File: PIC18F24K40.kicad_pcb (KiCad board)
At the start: 2 copper layers, 22 x 34.5 mm, 16 parts, among them J1 Conn_01x13, J2 Conn_01x13, J3 ICSP, J4 USB_B_Micro, SW1 SW_SPST, U1 FT231XQ, U2 PIC18F24K40-I_ML

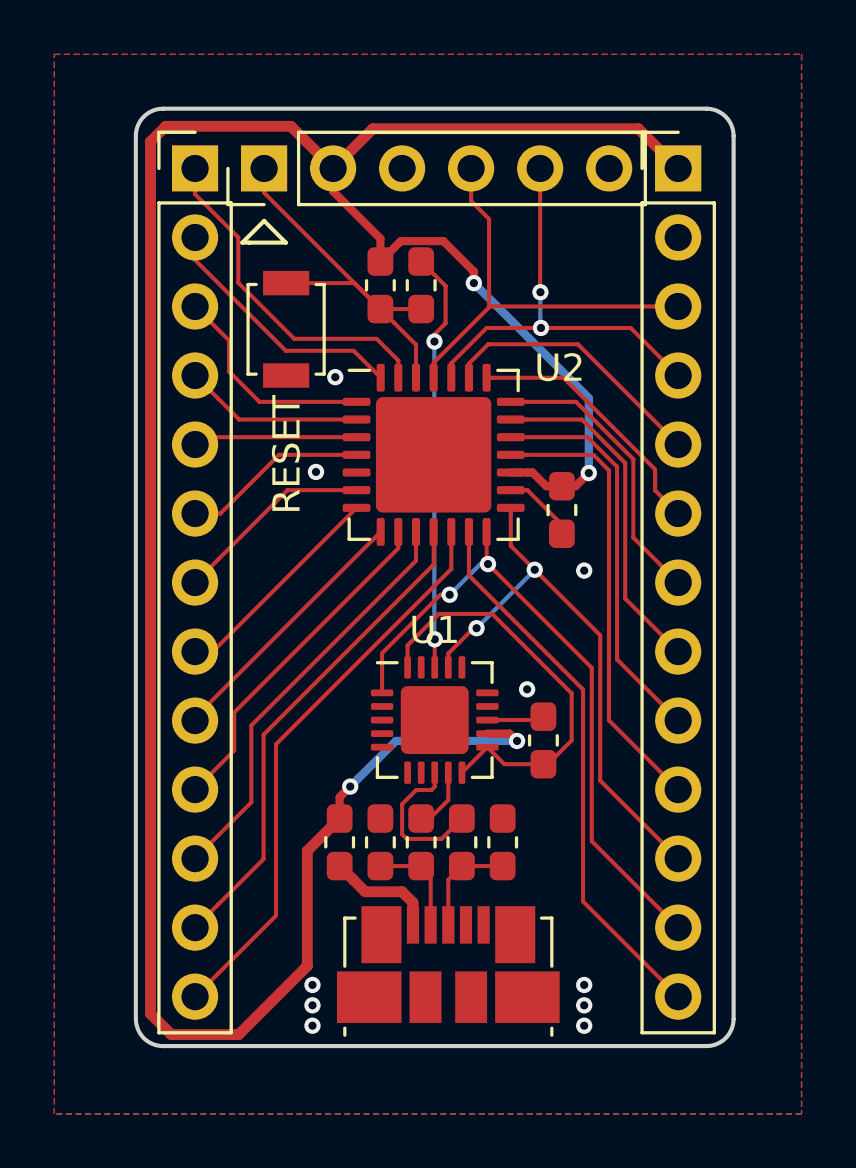
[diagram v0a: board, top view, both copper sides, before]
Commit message: LED and phototransistor added
I've added an LED for output and phototransistor for input. No button
though.
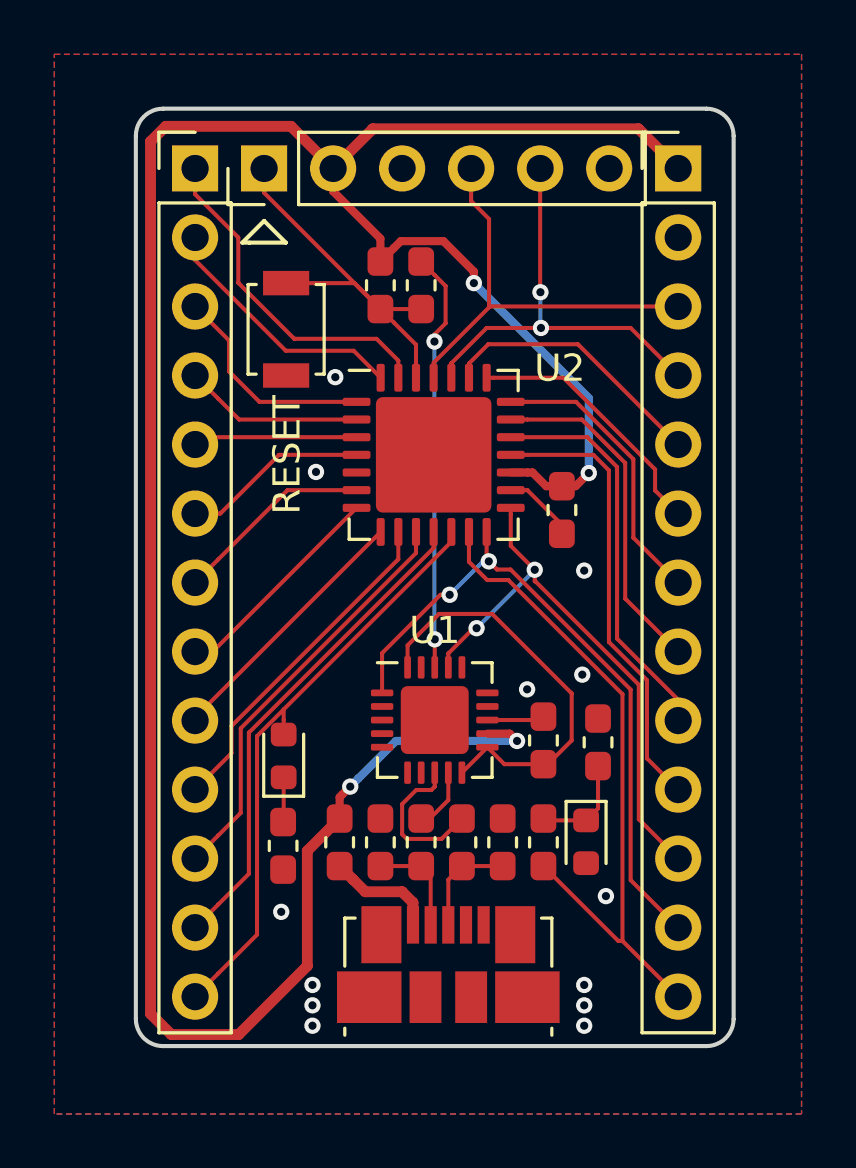
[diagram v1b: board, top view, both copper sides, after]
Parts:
- added C6: 0.01uf, _PIC18F24K40:C_0603_1608Metric_Pad1.05x0.95mm_HandSolder, F.Cu at (121.5, 97.3)
- added D1: blue, _PIC18F24K40:LED_0603_1608Metric, F.Cu at (109.9, 97.8)
- added Q1: Q_Photo_NPN, _PIC18F24K40:LED_0603_1608Metric, F.Cu at (121.1, 101.0)
- added R4: 360, _PIC18F24K40:R_0603_1608Metric_Pad1.05x0.95mm_HandSolder, F.Cu at (109.9, 101.1)
- added R5: 10k, _PIC18F24K40:R_0603_1608Metric_Pad1.05x0.95mm_HandSolder, F.Cu at (119.5, 101.0)
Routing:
- net /RC5: track 20.3 -> 24.8 mm
- net Net-(C6-Pad1): track 0.00 -> 3.78 mm
- net Net-(D1-Pad1): track 0.00 -> 1.66 mm
- net /RC4: track 21.0 -> 21.9 mm
- net GND: vias 10 -> 13

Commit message: Labels added to LED/Photo transistor
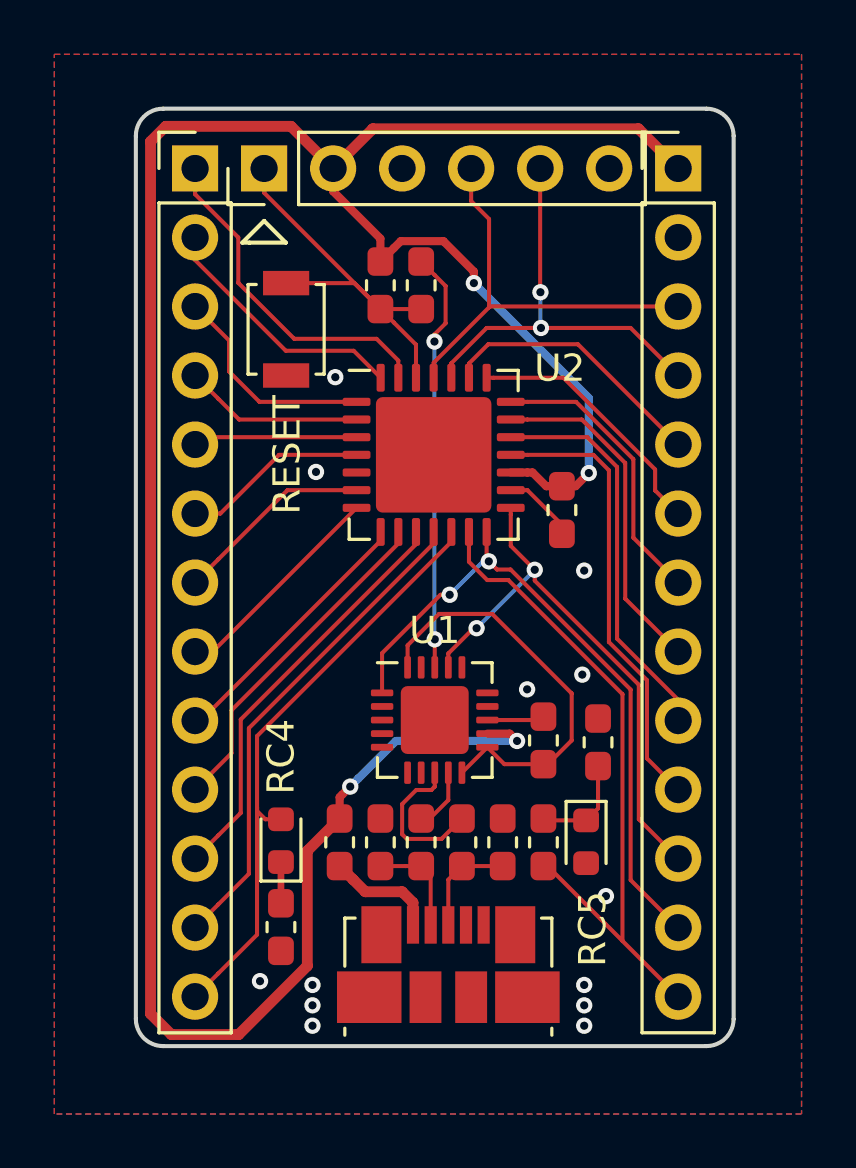
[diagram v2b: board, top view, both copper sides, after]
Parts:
- moved D1 3.12 mm to (109.8, 100.9)
- moved R4 2.99 mm to (109.8, 104.1)
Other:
- board text added: "RC4"
- board text added: "RC5"
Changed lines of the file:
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@@
   (general
     (thickness 1.6)
-    (drawings 9)
-    (tracks 253)
+    (drawings 11)
+    (tracks 256)
     (zones 0)
     (modules 21)
@@
   )
   (module _PIC18F24K40:LED_0603_1608Metric (layer F.Cu)
-    (at 109.94 97.82 90)
+    (at 109.84 100.94 90)
     (descr "LED SMD 0603 (1608 Metric), square (rectangular) end terminal, IPC_7351 nominal, (Body size source: http://www.tortai-tech.com/upload/download/2011102023233369053.pdf), generated with kicad-footprint-generator")
     (tags diode)
@@
   )
   (module _PIC18F24K40:R_0603_1608Metric_Pad1.05x0.95mm_HandSolder (layer F.Cu)
-    (at 109.92 101.13 270)
+    (at 109.84 104.12 270)
     (descr "Resistor SMD 0603 (1608 Metric), square (rectangular) end terminal, IPC_7351 nominal with elongated pad for handsoldering. (Body size source: http://www.tortai-tech.com/upload/download/2011102023233369053.pdf), generated with kicad-footprint-generator")
     (tags "resistor handsolder")
@@
       (rotate (xyz 0 0 0))
     )
+  )
+  (gr_text RC5 (at 121.31 104.19 90) (layer F.SilkS)
+    (effects (font (size 1 1) (thickness 0.15)))
+  )
+  (gr_text RC4 (at 109.84 97.85 90) (layer F.SilkS)
+    (effects (font (size 1 1) (thickness 0.15)))
   )
   (gr_arc (start 105.5 75) (end 105.5 74) (angle -90) (layer Edge.Cuts) (width 0.15))
@@
   (via (at 118.9 95.37) (size 0.6) (drill 0.3) (layers F.Cu B.Cu) (net 2))
   (via (at 111.84 83.88) (size 0.6) (drill 0.3) (layers F.Cu B.Cu) (net 2))
-  (via (at 109.85 103.56) (size 0.6) (drill 0.3) (layers F.Cu B.Cu) (net 2))
+  (via (at 109.07 106.11) (size 0.6) (drill 0.3) (layers F.Cu B.Cu) (net 2))
   (via (at 120.93 94.83) (size 0.6) (drill 0.3) (layers F.Cu B.Cu) (net 2))
   (via (at 121.8 102.98) (size 0.6) (drill 0.3) (layers F.Cu B.Cu) (net 2))
@@
   (segment (start 107.3325 93.98) (end 106.68 93.98) (width 0.15) (layer F.Cu) (net 8))
   (segment (start 112.6225 88.69) (end 107.3325 93.98) (width 0.15) (layer F.Cu) (net 8))
-  (segment (start 106.68 96.4075) (end 106.68 96.52) (width 0.15) (layer F.Cu) (net 9))
-  (segment (start 113.51 89.5775) (end 106.68 96.4075) (width 0.15) (layer F.Cu) (net 9))
+  (segment (start 106.89 96.52) (end 106.68 96.52) (width 0.15) (layer F.Cu) (net 9))
+  (segment (start 113.51 89.5775) (end 113.51 89.9) (width 0.15) (layer F.Cu) (net 9))
+  (segment (start 113.51 89.9) (end 106.89 96.52) (width 0.15) (layer F.Cu) (net 9))
   (segment (start 108.02 97.72) (end 106.68 99.06) (width 0.15) (layer F.Cu) (net 10))
-  (segment (start 108.02 96.721442) (end 108.02 97.72) (width 0.15) (layer F.Cu) (net 10))
-  (segment (start 114.16 89.5775) (end 114.16 90.581442) (width 0.15) (layer F.Cu) (net 10))
-  (segment (start 114.16 90.581442) (end 108.02 96.721442) (width 0.15) (layer F.Cu) (net 10))
-  (segment (start 114.81 89.5775) (end 114.81 90.355721) (width 0.15) (layer F.Cu) (net 11))
+  (segment (start 108.02 96.14) (end 108.02 97.72) (width 0.15) (layer F.Cu) (net 10))
+  (segment (start 114.16 89.5775) (end 114.16 90) (width 0.15) (layer F.Cu) (net 10))
+  (segment (start 114.16 90) (end 108.02 96.14) (width 0.15) (layer F.Cu) (net 10))
   (segment (start 107.529999 100.750001) (end 106.68 101.6) (width 0.15) (layer F.Cu) (net 11))
   (segment (start 108.359978 99.920022) (end 107.529999 100.750001) (width 0.15) (layer F.Cu) (net 11))
-  (segment (start 114.81 90.355721) (end 108.359978 96.805743) (width 0.15) (layer F.Cu) (net 11))
-  (segment (start 108.359978 96.805743) (end 108.359978 99.920022) (width 0.15) (layer F.Cu) (net 11))
+  (segment (start 114.81 89.5775) (end 114.81 90.03) (width 0.15) (layer F.Cu) (net 11))
+  (segment (start 108.359978 96.480022) (end 108.359978 99.920022) (width 0.15) (layer F.Cu) (net 11))
+  (segment (start 114.81 90.03) (end 108.359978 96.480022) (width 0.15) (layer F.Cu) (net 11))
   (segment (start 107.529999 103.290001) (end 106.68 104.14) (width 0.15) (layer F.Cu) (net 12))
+  (segment (start 108.659989 96.800011) (end 108.659989 102.160011) (width 0.15) (layer F.Cu) (net 12))
+  (segment (start 115.46 89.5775) (end 115.46 90) (width 0.15) (layer F.Cu) (net 12))
   (segment (start 108.659989 102.160011) (end 107.529999 103.290001) (width 0.15) (layer F.Cu) (net 12))
-  (segment (start 108.659989 96.965732) (end 108.659989 102.160011) (width 0.15) (layer F.Cu) (net 12))
-  (segment (start 115.46 89.5775) (end 115.46 90.165721) (width 0.15) (layer F.Cu) (net 12))
-  (segment (start 115.46 90.165721) (end 108.659989 96.965732) (width 0.15) (layer F.Cu) (net 12))
+  (segment (start 115.46 90) (end 108.659989 96.800011) (width 0.15) (layer F.Cu) (net 12))
   (segment (start 107.529999 105.830001) (end 106.68 106.68) (width 0.15) (layer F.Cu) (net 13))
   (segment (start 108.96 104.4) (end 107.529999 105.830001) (width 0.15) (layer F.Cu) (net 13))
-  (segment (start 108.96 97.09) (end 108.96 104.4) (width 0.15) (layer F.Cu) (net 13))
-  (segment (start 116.11 89.5775) (end 116.11 89.94) (width 0.15) (layer F.Cu) (net 13))
-  (segment (start 109.94 96.495) (end 109.94 96.11) (width 0.15) (layer F.Cu) (net 13))
-  (segment (start 109.94 97.0325) (end 109.94 96.495) (width 0.15) (layer F.Cu) (net 13))
-  (segment (start 116.11 89.94) (end 109.94 96.11) (width 0.15) (layer F.Cu) (net 13))
-  (segment (start 109.94 96.11) (end 108.96 97.09) (width 0.15) (layer F.Cu) (net 13))
   (segment (start 122.41 95.55) (end 122.41 104.63) (width 0.15) (layer F.Cu) (net 14))
   (segment (start 117.43 91.347004) (end 118.207004 91.347004) (width 0.15) (layer F.Cu) (net 14))
@@
   (segment (start 116.76 89.5775) (end 116.76 90.677004) (width 0.15) (layer F.Cu) (net 14))
   (segment (start 116.76 90.677004) (end 117.43 91.347004) (width 0.15) (layer F.Cu) (net 14))
-  (segment (start 122.255 104.63) (end 122.41 104.63) (width 0.15) (layer F.Cu) (net 14))
-  (segment (start 119.5 101.875) (end 122.255 104.63) (width 0.15) (layer F.Cu) (net 14))
+  (segment (start 121.77 103.99) (end 122.41 104.63) (width 0.15) (layer F.Cu) (net 14))
+  (segment (start 119.5 101.875) (end 119.655 101.875) (width 0.15) (layer F.Cu) (net 14))
+  (segment (start 119.655 101.875) (end 121.77 103.99) (width 0.15) (layer F.Cu) (net 14))
   (via (at 116.05 91.89) (size 0.6) (drill 0.3) (layers F.Cu B.Cu) (net 15))
   (segment (start 115.71 91.89) (end 116.05 91.89) (width 0.15) (layer F.Cu) (net 15))
@@
   (segment (start 117.04 93.12) (end 119.18 90.98) (width 0.15) (layer B.Cu) (net 16))
   (segment (start 119.18 90.97) (end 118.2975 90.0875) (width 0.15) (layer F.Cu) (net 16))
-  (segment (start 119.18 91.394264) (end 119.18 90.97) (width 0.15) (layer F.Cu) (net 16))
-  (segment (start 119.204264 91.394264) (end 119.18 91.394264) (width 0.15) (layer F.Cu) (net 16))
-  (segment (start 123.010022 95.200022) (end 119.204264 91.394264) (width 0.15) (layer F.Cu) (net 16))
+  (segment (start 123.010022 95.200022) (end 119.18 91.37) (width 0.15) (layer F.Cu) (net 16))
   (segment (start 124.46 101.6) (end 123.010022 100.150022) (width 0.15) (layer F.Cu) (net 16))
+  (segment (start 119.18 91.37) (end 119.18 90.97) (width 0.15) (layer F.Cu) (net 16))
   (segment (start 123.010022 100.150022) (end 123.010022 95.200022) (width 0.15) (layer F.Cu) (net 16))
   (segment (start 118.91 86.74) (end 118.2975 86.74) (width 0.15) (layer F.Cu) (net 17))
@@
   (segment (start 114.7 104.04) (end 114.7 103.22) (width 0.4) (layer F.Cu) (net 45))
   (segment (start 114.7 103.22) (end 114.3 102.82) (width 0.4) (layer F.Cu) (net 45))
-  (segment (start 109.94 100.235) (end 109.92 100.255) (width 0.15) (layer F.Cu) (net 46))
-  (segment (start 109.94 98.6075) (end 109.94 100.235) (width 0.15) (layer F.Cu) (net 46))
+  (segment (start 109.94 100.235) (end 109.92 100.255) (width 0.15) (layer F.Cu) (net 13))
+  (segment (start 108.96 99.8475) (end 108.96 99.72) (width 0.15) (layer F.Cu) (net 13))
+  (segment (start 109.84 100.1525) (end 109.265 100.1525) (width 0.15) (layer F.Cu) (net 13))
+  (segment (start 109.265 100.1525) (end 108.96 99.8475) (width 0.15) (layer F.Cu) (net 13))
+  (segment (start 108.96 99.72) (end 108.96 104.4) (width 0.15) (layer F.Cu) (net 13))
+  (segment (start 108.96 98.0125) (end 108.96 99.72) (width 0.15) (layer F.Cu) (net 13))
+  (segment (start 116.11 89.5775) (end 116.11 89.94) (width 0.15) (layer F.Cu) (net 13))
+  (segment (start 108.96 97.09) (end 108.96 98.0125) (width 0.15) (layer F.Cu) (net 13))
+  (segment (start 116.11 89.94) (end 108.96 97.09) (width 0.15) (layer F.Cu) (net 13))
+  (segment (start 109.84 103.245) (end 109.84 101.7275) (width 0.25) (layer F.Cu) (net 46))
   (segment (start 121.51 99.7525) (end 121.07 100.1925) (width 0.15) (layer F.Cu) (net 47))
   (segment (start 121.51 98.195) (end 121.51 99.7525) (width 0.15) (layer F.Cu) (net 47))
